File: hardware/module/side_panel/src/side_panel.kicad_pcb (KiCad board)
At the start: 2 copper layers, 96 x 120.2 mm, 45 parts, among them J1 Top Connector, J2 Bottom Connecor, J3 Conn_01x05, J4 Conn_01x09, M1 GA12-N20 12V 100rpm, Q1 AP2302B, U1 QRE1113GR, U2 QRE1113GR, U3 QRE1113GR, U4 QRE1113GR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

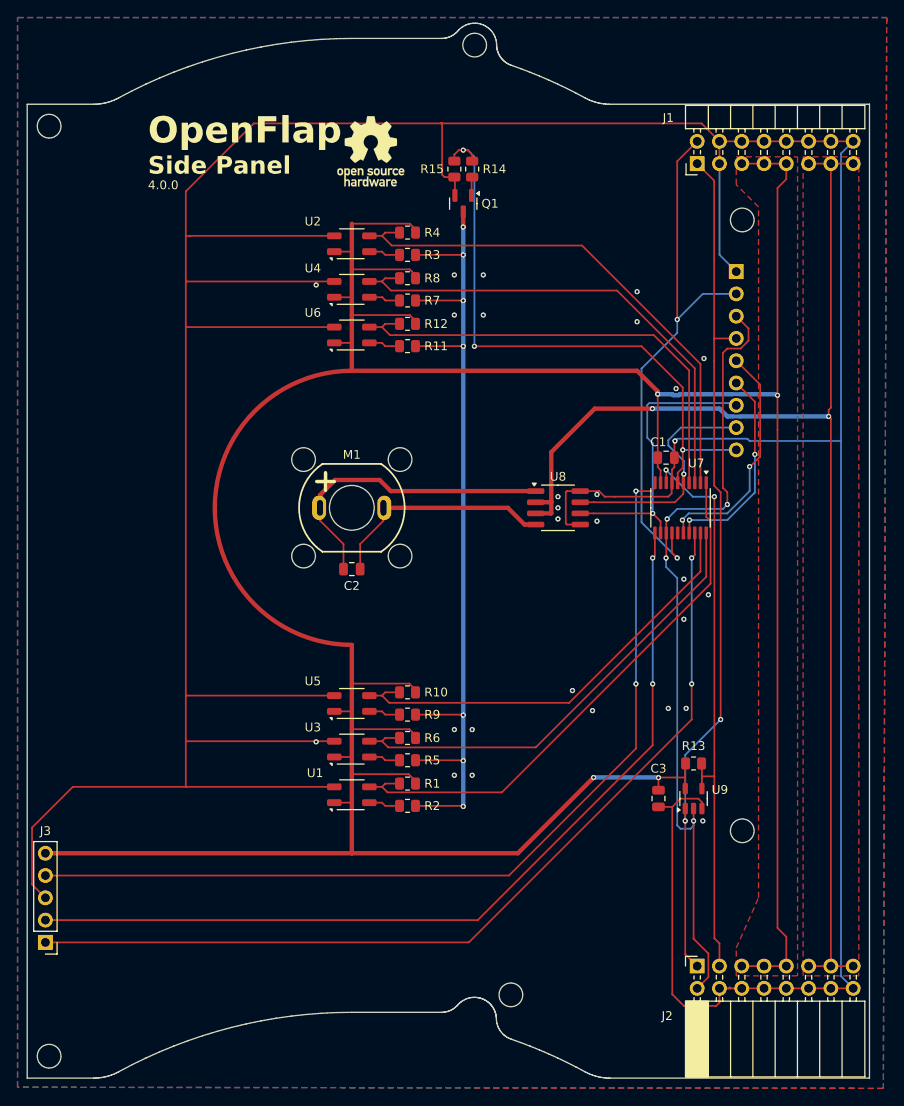
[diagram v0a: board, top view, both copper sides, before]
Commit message: Add FreeCad model and update board layout.
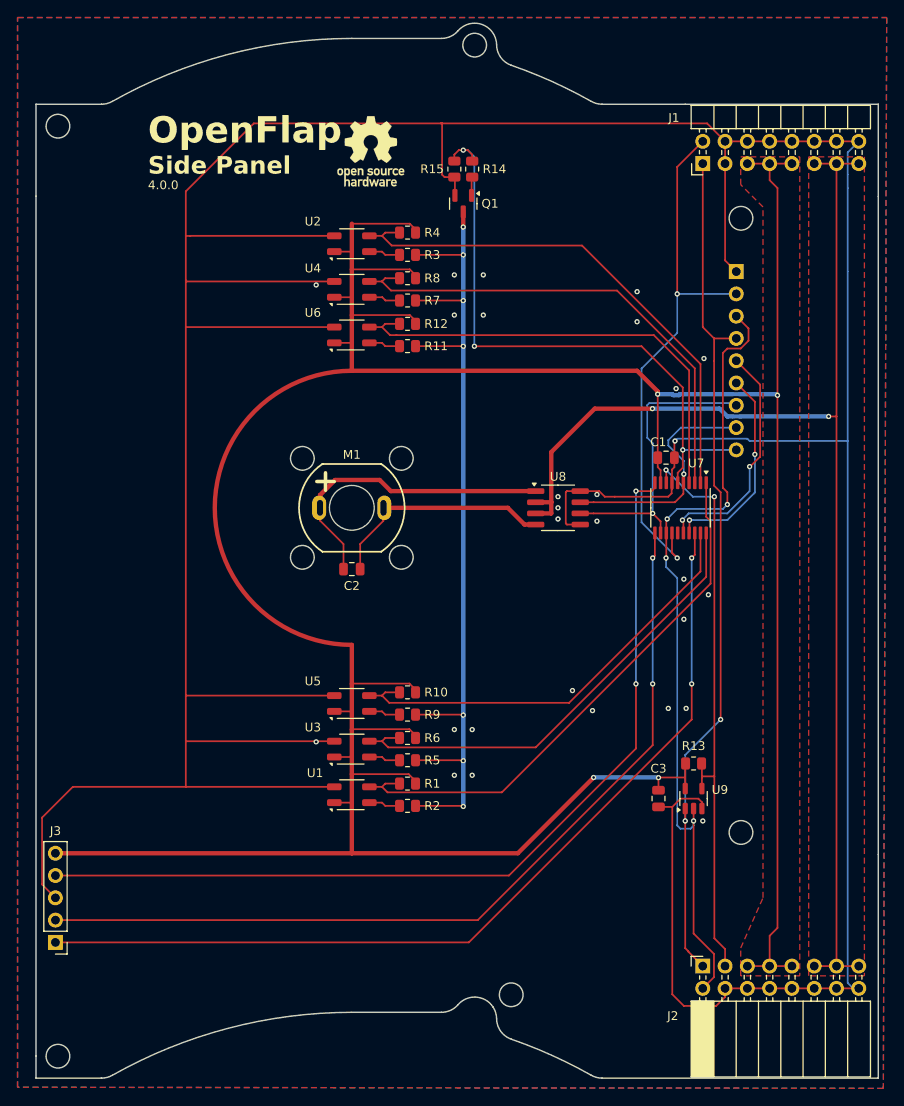
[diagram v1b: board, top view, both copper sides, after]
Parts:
- removed H1, H10, H2, H3, H4, H5, H6, H7, H8, H9: MountingHole, MountingHole:MountingHole_2.7mm_M2.5_ISO14580
- moved J3 1.14 mm to (63.2, 181.7)
- moved J1 0.64 mm to (136.9, 93.0)
- moved J2 0.64 mm to (136.9, 184.4)
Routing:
- net +5V: track 343.7 -> 342.5 mm
- net /~{RST}: track 105.6 -> 104.5 mm
- net /SWD: track 105.5 -> 104.4 mm
- net /SWC: track 101.8 -> 100.6 mm
- net /RX Top: track 63.0 -> 62.0 mm
- net +12V: track 146.4 -> 147.1 mm
- net GND: track 494.7 -> 495.2 mm
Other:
- outline, holes or cut-outs redrawn

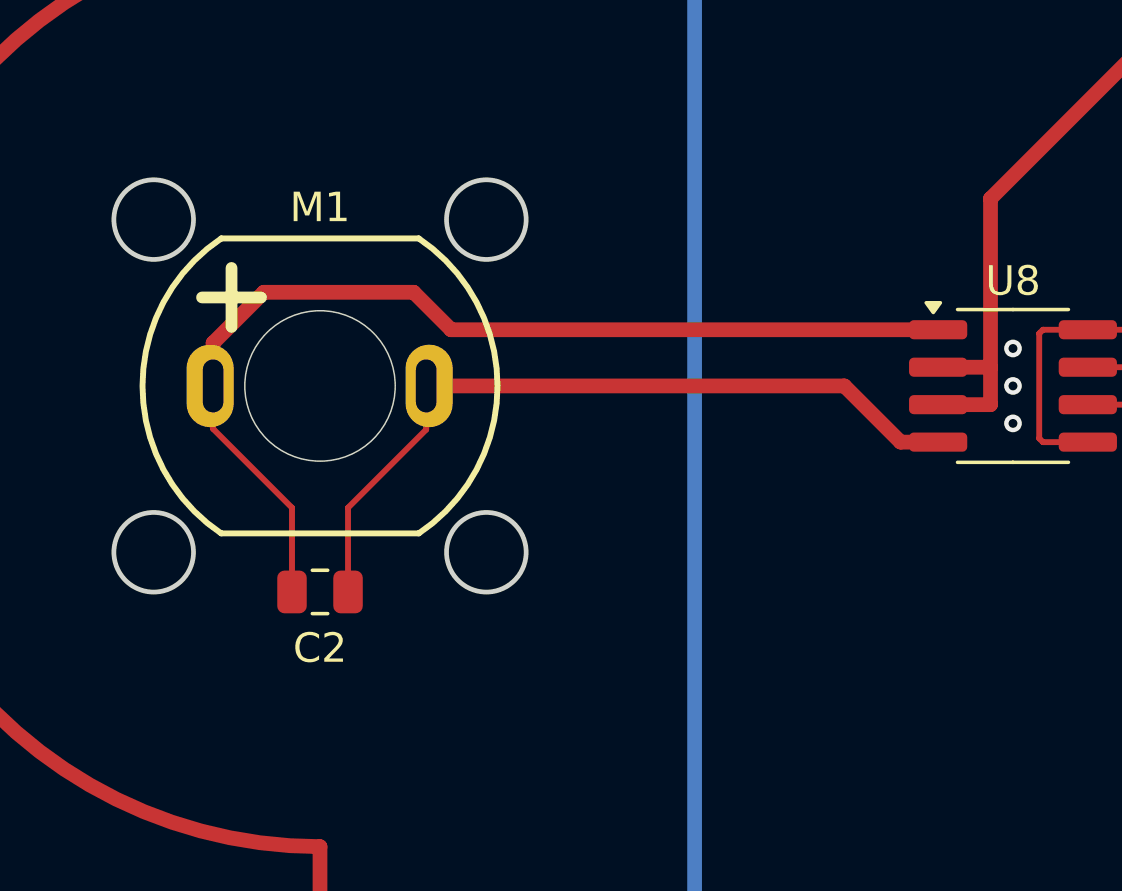
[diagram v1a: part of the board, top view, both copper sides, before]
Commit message: Updated Motor footprint
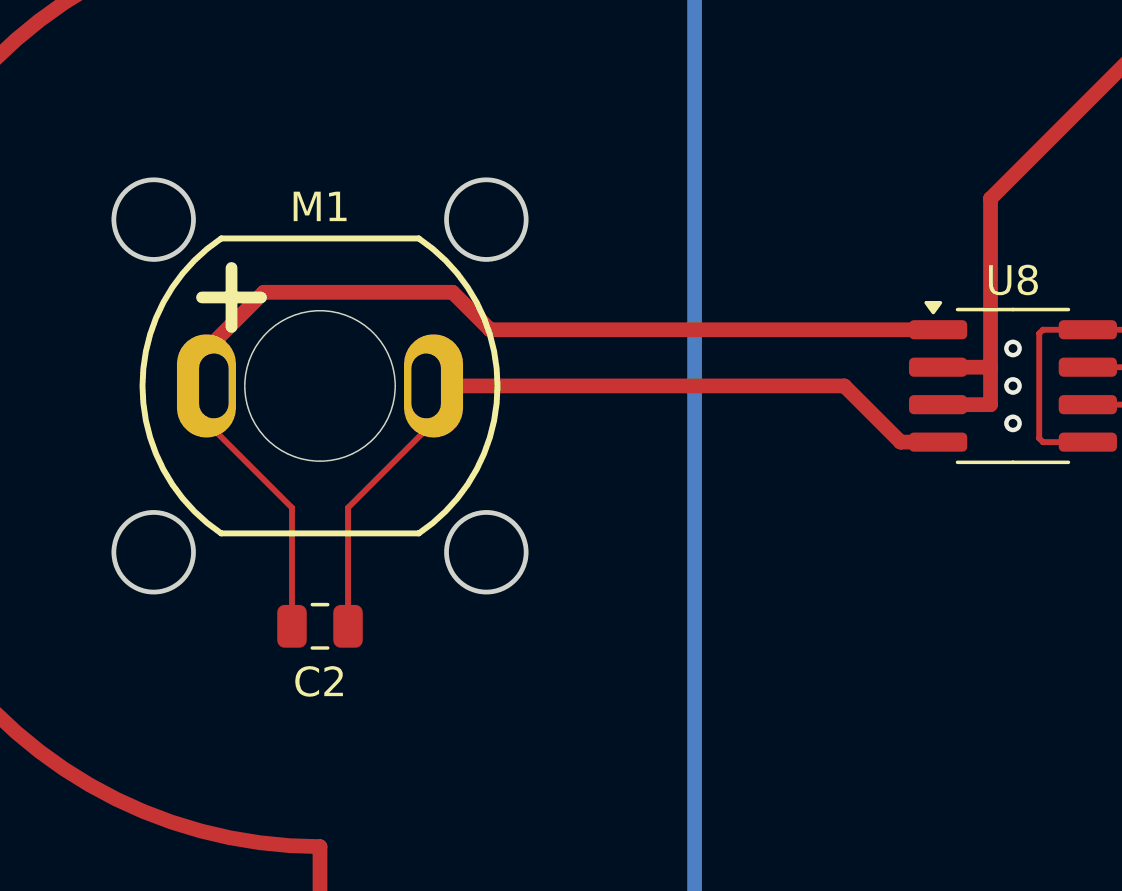
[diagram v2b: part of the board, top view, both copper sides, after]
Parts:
- moved C2 1.16 mm to (96.9, 140.3)
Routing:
- net Net-(M1-+): track 35.4 -> 38.0 mm
- net Net-(M1--): track 26.2 -> 27.4 mm
